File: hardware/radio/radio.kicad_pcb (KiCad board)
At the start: 2 copper layers, 48 parts, among them P101 CONN_01X04, P102 CONN_02X03, P103 CONN_02X05, P104 CONN_01X02, Q301 Q_NMOS_DGS, U201 LTC3331, X301 8MHz

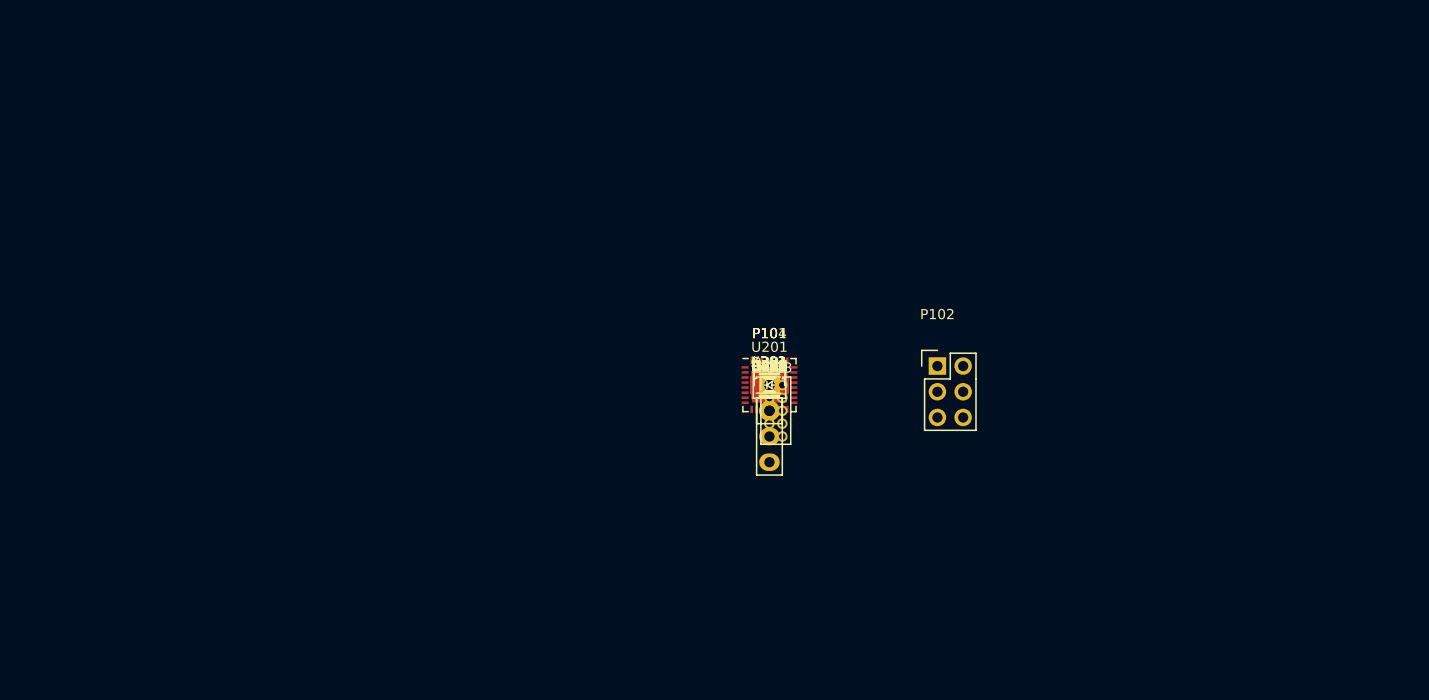
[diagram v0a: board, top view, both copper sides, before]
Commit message: Draw PCB outline
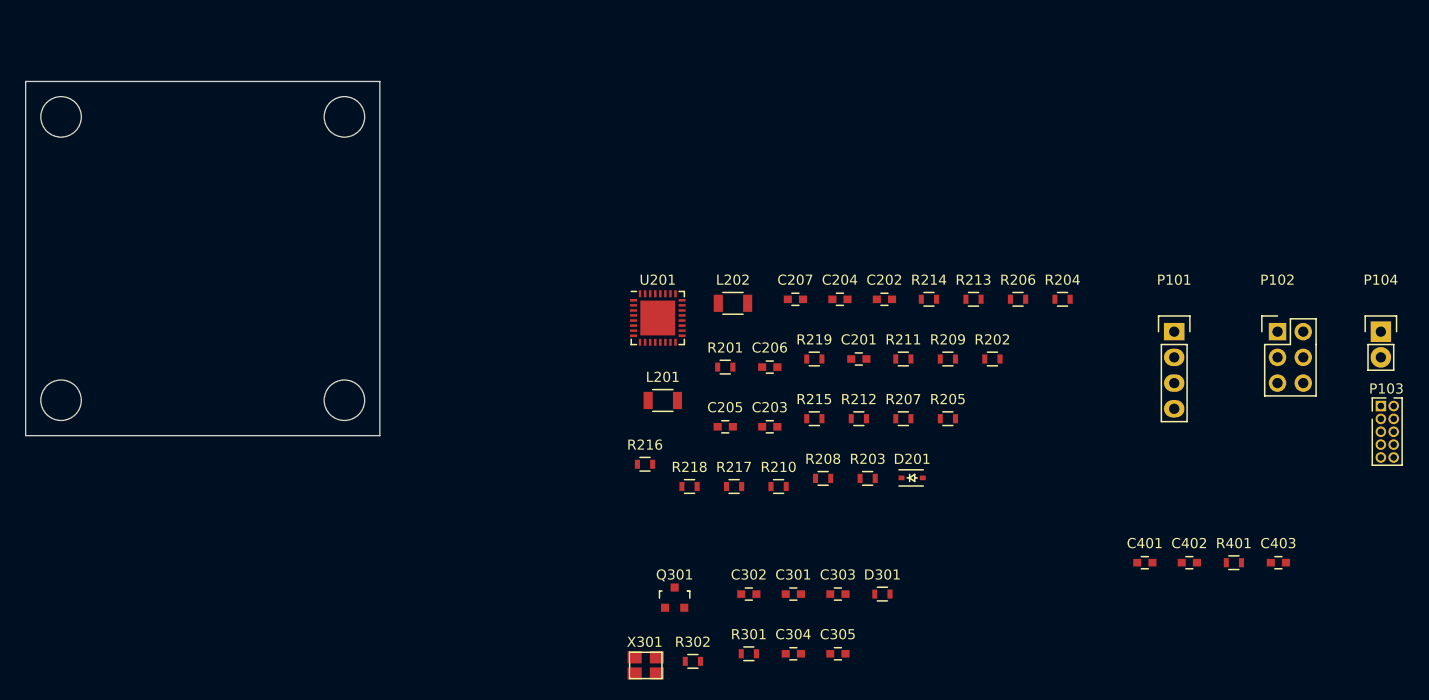
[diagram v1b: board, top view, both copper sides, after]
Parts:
- moved P104 60.6 mm to (208.9, 99.7)
- moved P103 60.5 mm to (208.9, 107.1)
- moved C403 53.3 mm to (198.8, 122.6)
- moved R401 49.1 mm to (194.4, 122.6)
- moved C402 45.1 mm to (190.0, 122.6)
- moved C401 41.0 mm to (185.6, 122.6)
- moved P101 40.3 mm to (188.5, 99.7)
- moved P102 33.8 mm to (198.7, 99.7)
- moved X301 30.3 mm to (136.3, 132.7)
- moved R204 30.2 mm to (177.5, 96.5)
- moved R302 28.3 mm to (140.9, 132.3)
- moved C305 27.4 mm to (155.3, 131.6)
- moved C304 26.7 mm to (150.9, 131.6)
- moved R301 26.6 mm to (146.5, 131.6)
- moved R206 26.0 mm to (173.1, 96.5)
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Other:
- board outline added: 35 x 35 mm

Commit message: Add radio footprint to PCB
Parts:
- added IC301: ATMEGA328-P, Housings_QFP:TQFP-32_7x7mm_Pitch0.8mm, F.Cu at (92.5, 120.1)
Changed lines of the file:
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@@
-(kicad_pcb (version 4) (host pcbnew "(2015-07-08 BZR 5908, Git 901e961)-product")
+(kicad_pcb (version 4) (host pcbnew "(2015-07-10 BZR 5924)-product")
   (general
-    (links 97)
-    (no_connects 97)
+    (links 112)
+    (no_connects 112)
     (area 74.949999 74.949999 110.050001 110.050001)
     (thickness 1.6)
@@
     (tracks 0)
     (zones 0)
-    (modules 48)
-    (nets 50)
+    (modules 49)
+    (nets 63)
   )
   (page A4)
@@
   (net 48 /Control/UV0)
   (net 49 "Net-(U201-Pad10)")
+  (net 50 /Control/RX)
+  (net 51 /Bluetooth/RXD)
+  (net 52 /Control/INT0)
+  (net 53 /Control/INT1)
+  (net 54 "Net-(IC301-Pad12)")
+  (net 55 "Net-(IC301-Pad13)")
+  (net 56 "Net-(IC301-Pad14)")
+  (net 57 /Control/SPI_SS)
+  (net 58 "Net-(IC301-Pad24)")
+  (net 59 "Net-(IC301-Pad25)")
+  (net 60 "Net-(IC301-Pad26)")
+  (net 61 "Net-(IC301-Pad27)")
+  (net 62 "Net-(IC301-Pad28)")
   (net_class Default "This is the default net class."
     (clearance 0.2)
@@
     (add_net /Bluetooth/P2_1-PROG)
     (add_net /Bluetooth/P2_2-PROG)
+    (add_net /Bluetooth/RXD)
     (add_net /Control/BLE_RS)
     (add_net /Control/EH_ON)
+    (add_net /Control/INT0)
+    (add_net /Control/INT1)
     (add_net /Control/MISO)
     (add_net /Control/MOSI)
     (add_net /Control/RESET)
+    (add_net /Control/RX)
     (add_net /Control/SCK)
+    (add_net /Control/SPI_SS)
     (add_net /Control/SW_RX)
     (add_net /Control/SW_TX)
@@
     (add_net "Net-(D301-Pad1)")
     (add_net "Net-(D301-Pad2)")
+    (add_net "Net-(IC301-Pad12)")
+    (add_net "Net-(IC301-Pad13)")
+    (add_net "Net-(IC301-Pad14)")
+    (add_net "Net-(IC301-Pad24)")
+    (add_net "Net-(IC301-Pad25)")
+    (add_net "Net-(IC301-Pad26)")
+    (add_net "Net-(IC301-Pad27)")
+    (add_net "Net-(IC301-Pad28)")
     (add_net "Net-(L201-Pad2)")
     (add_net "Net-(L202-Pad1)")
@@
     )
   )
+  (module Housings_QFP:TQFP-32_7x7mm_Pitch0.8mm (layer F.Cu)
+    (at 92.5 120.050001)
+    (descr "32-Lead Plastic Thin Quad Flatpack (PT) - 7x7x1.0 mm Body, 2.00 mm [TQFP] (see Microchip Packaging Specification 00000049BS.pdf)")
+    (tags "QFP 0.8")
+    (attr smd)
+    (fp_text reference IC301 (at 0 -6.05) (layer F.SilkS)
+      (effects (font (size 1 1) (thickness 0.15)))
+    )
+    (fp_text value ATMEGA328-P (at 0 6.05) (layer F.Fab)
+      (effects (font (size 1 1) (thickness 0.15)))
+    )
+    (fp_line (start -5.3 -5.3) (end -5.3 5.3) (layer F.CrtYd) (width 0.05))
+    (fp_line (start 5.3 -5.3) (end 5.3 5.3) (layer F.CrtYd) (width 0.05))
+    (fp_line (start -5.3 -5.3) (end 5.3 -5.3) (layer F.CrtYd) (width 0.05))
+    (fp_line (start -5.3 5.3) (end 5.3 5.3) (layer F.CrtYd) (width 0.05))
+    (fp_line (start -3.625 -3.625) (end -3.625 -3.3) (layer F.SilkS) (width 0.15))
+    (fp_line (start 3.625 -3.625) (end 3.625 -3.3) (layer F.SilkS) (width 0.15))
+    (fp_line (start 3.625 3.625) (end 3.625 3.3) (layer F.SilkS) (width 0.15))
+    (fp_line (start -3.625 3.625) (end -3.625 3.3) (layer F.SilkS) (width 0.15))
+    (fp_line (start -3.625 -3.625) (end -3.3 -3.625) (layer F.SilkS) (width 0.15))
+    (fp_line (start -3.625 3.625) (end -3.3 3.625) (layer F.SilkS) (width 0.15))
+    (fp_line (start 3.625 3.625) (end 3.3 3.625) (layer F.SilkS) (width 0.15))
+    (fp_line (start 3.625 -3.625) (end 3.3 -3.625) (layer F.SilkS) (width 0.15))
+    (fp_line (start -3.625 -3.3) (end -5.05 -3.3) (layer F.SilkS) (width 0.15))
+    (pad 1 smd rect (at -4.25 -2.8) (size 1.6 0.55) (layers F.Cu F.Paste F.Mask)
+      (net 12 /Control/RESET))
+    (pad 2 smd rect (at -4.25 -2) (size 1.6 0.55) (layers F.Cu F.Paste F.Mask)
+      (net 50 /Control/RX))
+    (pad 3 smd rect (at -4.25 -1.2) (size 1.6 0.55) (layers F.Cu F.Paste F.Mask)
+      (net 51 /Bluetooth/RXD))
+    (pad 4 smd rect (at -4.25 -0.4) (size 1.6 0.55) (layers F.Cu F.Paste F.Mask)
+      (net 52 /Control/INT0))
+    (pad 5 smd rect (at -4.25 0.4) (size 1.6 0.55) (layers F.Cu F.Paste F.Mask)
+      (net 53 /Control/INT1))
+    (pad 6 smd rect (at -4.25 1.2) (size 1.6 0.55) (layers F.Cu F.Paste F.Mask)
+      (net 25 /Control/BLE_RS))
+    (pad 7 smd rect (at -4.25 2) (size 1.6 0.55) (layers F.Cu F.Paste F.Mask)
+      (net 4 VCC))
+    (pad 8 smd rect (at -4.25 2.8) (size 1.6 0.55) (layers F.Cu F.Paste F.Mask)
+      (net 3 GND))
+    (pad 9 smd rect (at -2.8 4.25 90) (size 1.6 0.55) (layers F.Cu F.Paste F.Mask)
+      (net 10 "Net-(C303-Pad1)"))
+    (pad 10 smd rect (at -2 4.25 90) (size 1.6 0.55) (layers F.Cu F.Paste F.Mask)
+      (net 11 "Net-(C304-Pad1)"))
+    (pad 11 smd rect (at -1.2 4.25 90) (size 1.6 0.55) (layers F.Cu F.Paste F.Mask)
+      (net 16 "Net-(D301-Pad2)"))
+    (pad 12 smd rect (at -0.4 4.25 90) (size 1.6 0.55) (layers F.Cu F.Paste F.Mask)
+      (net 54 "Net-(IC301-Pad12)"))
+    (pad 13 smd rect (at 0.4 4.25 90) (size 1.6 0.55) (layers F.Cu F.Paste F.Mask)
+      (net 55 "Net-(IC301-Pad13)"))
+    (pad 14 smd rect (at 1.2 4.25 90) (size 1.6 0.55) (layers F.Cu F.Paste F.Mask)
+      (net 56 "Net-(IC301-Pad14)"))
+    (pad 15 smd rect (at 2 4.25 90) (size 1.6 0.55) (layers F.Cu F.Paste F.Mask)
+      (net 57 /Control/SPI_SS))
+    (pad 16 smd rect (at 2.8 4.25 90) (size 1.6 0.55) (layers F.Cu F.Paste F.Mask)
+      (net 20 /Control/SW_RX))
+    (pad 17 smd rect (at 4.25 2.8) (size 1.6 0.55) (layers F.Cu F.Paste F.Mask)
+      (net 24 /Control/MOSI))
+    (pad 18 smd rect (at 4.25 2) (size 1.6 0.55) (layers F.Cu F.Paste F.Mask)
+      (net 22 /Control/MISO))
+    (pad 19 smd rect (at 4.25 1.2) (size 1.6 0.55) (layers F.Cu F.Paste F.Mask)
+      (net 23 /Control/SCK))
+    (pad 20 smd rect (at 4.25 0.4) (size 1.6 0.55) (layers F.Cu F.Paste F.Mask)
+      (net 4 VCC))
+    (pad 21 smd rect (at 4.25 -0.4) (size 1.6 0.55) (layers F.Cu F.Paste F.Mask)
+      (net 9 "Net-(C302-Pad1)"))
+    (pad 22 smd rect (at 4.25 -1.2) (size 1.6 0.55) (layers F.Cu F.Paste F.Mask)
+      (net 3 GND))
+    (pad 23 smd rect (at 4.25 -2) (size 1.6 0.55) (layers F.Cu F.Paste F.Mask)
+      (net 21 /Control/SW_TX))
+    (pad 24 smd rect (at 4.25 -2.8) (size 1.6 0.55) (layers F.Cu F.Paste F.Mask)
+      (net 58 "Net-(IC301-Pad24)"))
+    (pad 25 smd rect (at 2.8 -4.25 90) (size 1.6 0.55) (layers F.Cu F.Paste F.Mask)
+      (net 59 "Net-(IC301-Pad25)"))
+    (pad 26 smd rect (at 2 -4.25 90) (size 1.6 0.55) (layers F.Cu F.Paste F.Mask)
+      (net 60 "Net-(IC301-Pad26)"))
+    (pad 27 smd rect (at 1.2 -4.25 90) (size 1.6 0.55) (layers F.Cu F.Paste F.Mask)
+      (net 61 "Net-(IC301-Pad27)"))
+    (pad 28 smd rect (at 0.4 -4.25 90) (size 1.6 0.55) (layers F.Cu F.Paste F.Mask)
+      (net 62 "Net-(IC301-Pad28)"))
+    (pad 29 smd rect (at -0.4 -4.25 90) (size 1.6 0.55) (layers F.Cu F.Paste F.Mask))
+    (pad 30 smd rect (at -1.2 -4.25 90) (size 1.6 0.55) (layers F.Cu F.Paste F.Mask))
+    (pad 31 smd rect (at -2 -4.25 90) (size 1.6 0.55) (layers F.Cu F.Paste F.Mask))
+    (pad 32 smd rect (at -2.8 -4.25 90) (size 1.6 0.55) (layers F.Cu F.Paste F.Mask))
+    (model Housings_QFP.3dshapes/TQFP-32_7x7mm_Pitch0.8mm.wrl
+      (at (xyz 0 0 0))
+      (scale (xyz 1 1 1))
+      (rotate (xyz 0 0 0))
+    )
+  )

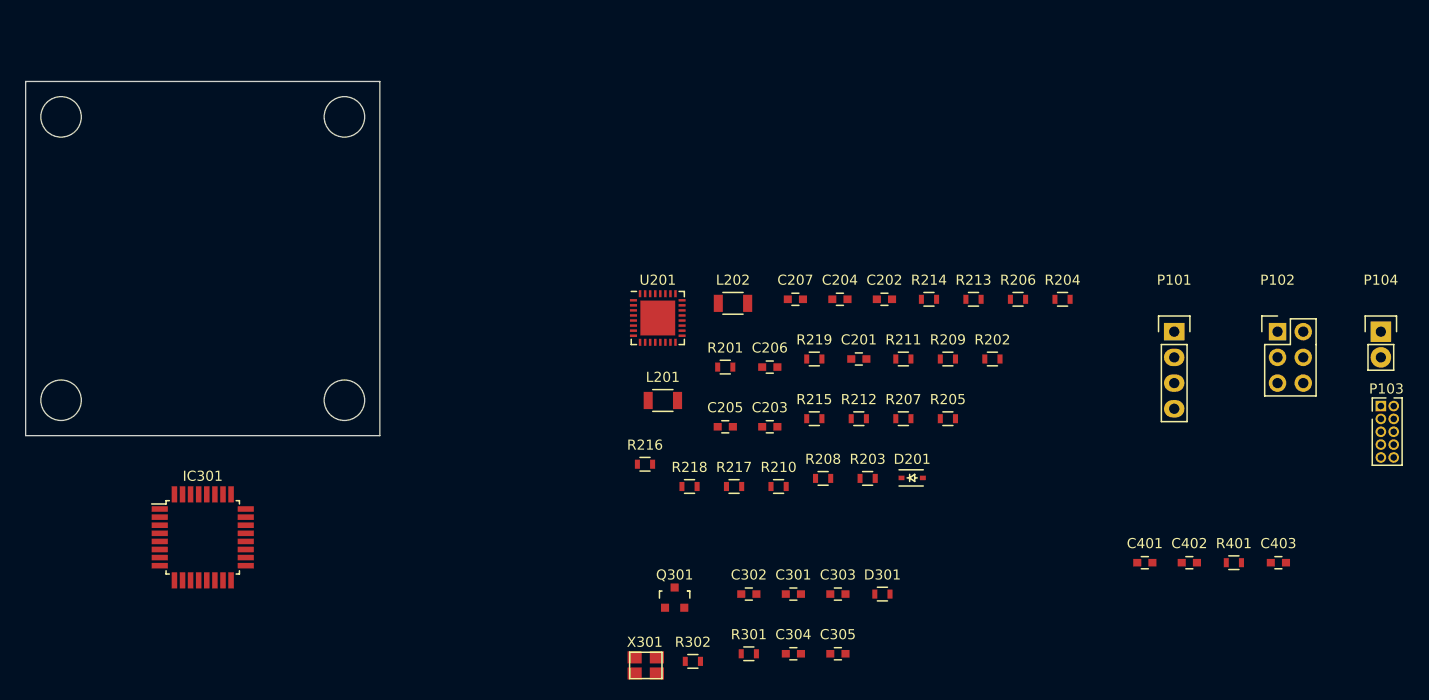
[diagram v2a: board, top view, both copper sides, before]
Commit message: Add accelerometer to schematic
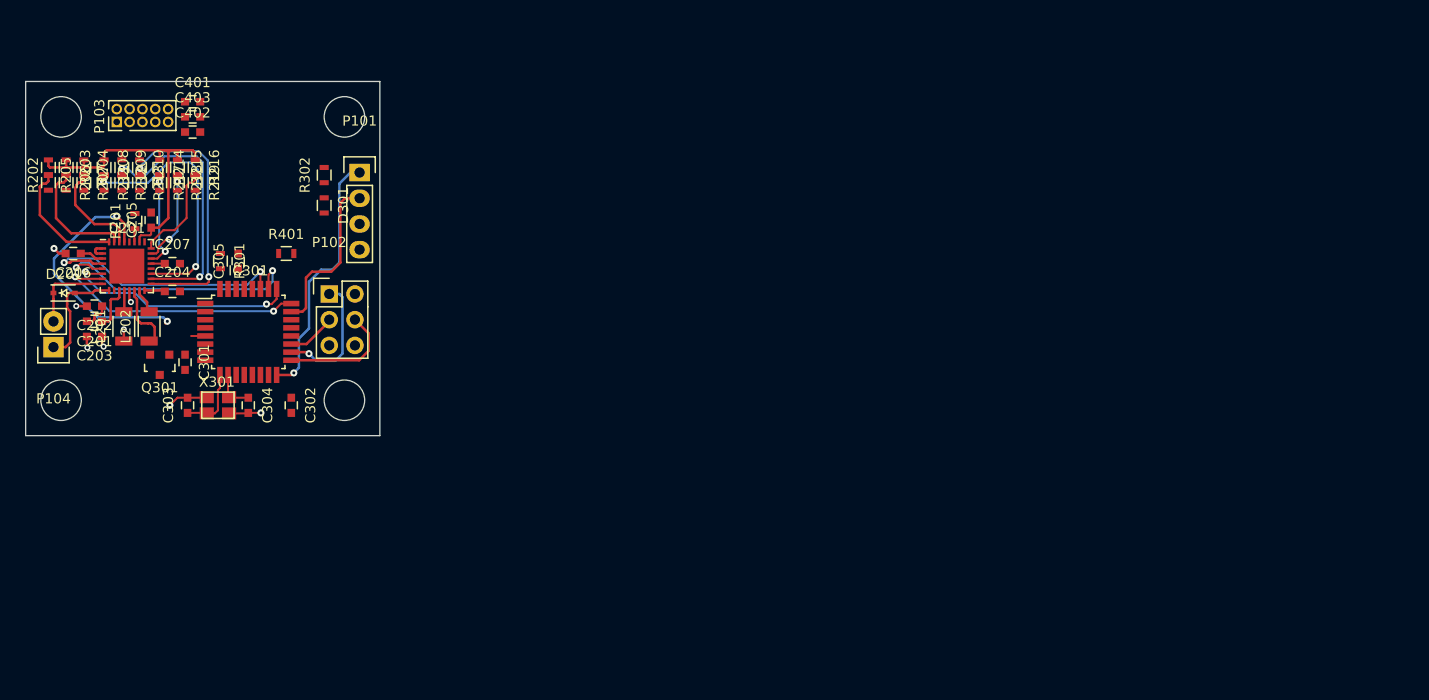
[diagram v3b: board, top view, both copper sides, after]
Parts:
- moved P104 131.2 mm to (77.8, 101.2), turned to 180 degrees
- moved P103 128.0 mm to (84.0, 79.0), turned to 90 degrees
- moved C403 116.0 mm to (91.5, 78.5)
- moved C402 107.3 mm to (91.5, 80.0)
- moved C401 104.5 mm to (91.5, 77.0)
- moved R401 98.5 mm to (100.8, 92.0)
- moved R204 97.6 mm to (80.8, 83.5), turned to 270 degrees
- moved R202 95.2 mm to (77.2, 83.5), turned to 270 degrees
- moved R206 94.8 mm to (79.0, 85.0), turned to 270 degrees
- moved P102 93.8 mm to (105.0, 96.0)
- moved R205 91.9 mm to (77.2, 85.0), turned to 270 degrees
- moved D201 85.8 mm to (78.8, 95.9)
- moved R203 85.0 mm to (79.0, 83.5), turned to 270 degrees
- moved R207 84.3 mm to (80.8, 85.0), turned to 270 degrees
- moved R209 83.8 mm to (84.5, 83.5), turned to 270 degrees
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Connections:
- IC301 pad 24: Net-(IC301-Pad24) -> /Control/UV0
- IC301 pad 25: Net-(IC301-Pad25) -> /Control/UV1
- IC301 pad 26: Net-(IC301-Pad26) -> /Control/UV2
- IC301 pad 27: Net-(IC301-Pad27) -> /Control/UV3
- Q301 pad 1: Net-(Q301-Pad1) -> /Control/INT1
- U201 pad 10: Net-(U201-Pad10) -> Net-(C201-Pad2)
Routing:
- net /Power management/VIN3: track 0.00 -> 35.2 mm
- net /Control/UV3: track 0.00 -> 27.2 mm, vias 0 -> 2
- net /Control/UV2: track 0.00 -> 27.0 mm, vias 0 -> 2
- net /Power management/IPK1: track 0.00 -> 26.4 mm, vias 0 -> 2
- net /Power management/IPK0: track 0.00 -> 26.4 mm, vias 0 -> 2
- net /Control/UV0: track 0.00 -> 25.9 mm, vias 0 -> 2
- net /Control/EH_ON: track 0.00 -> 25.7 mm, vias 0 -> 2
- net /Power management/IPK2: track 0.00 -> 25.5 mm, vias 0 -> 2
- net /Control/SW_RX: track 0.00 -> 25.4 mm, vias 0 -> 1
- net /Control/UV1: track 0.00 -> 23.7 mm, vias 0 -> 2
- net /Control/SW_TX: track 0.00 -> 16.6 mm
- net /Control/MISO: track 0.00 -> 12.7 mm, vias 0 -> 1
- net /Power management/OUT2: track 0.00 -> 12.4 mm
- net /Power management/OUT1: track 0.00 -> 12.2 mm
- net /Control/MOSI: track 0.00 -> 11.7 mm
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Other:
- copper layers 2 -> 4
- net class Default: clearance 0.2 -> 0.17; via_drill 0.4 -> 0.3
- rule trace_clearance: 0.2 -> 0.17
- rule trace_min: 0.2 -> 0.15
- rule via_min_size: 0.4 -> 0.6
